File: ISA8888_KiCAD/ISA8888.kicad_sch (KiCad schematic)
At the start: 3 parts, among them J1 Bus_PCI_32bit_Universal, J2 Bus_ISA_16bit

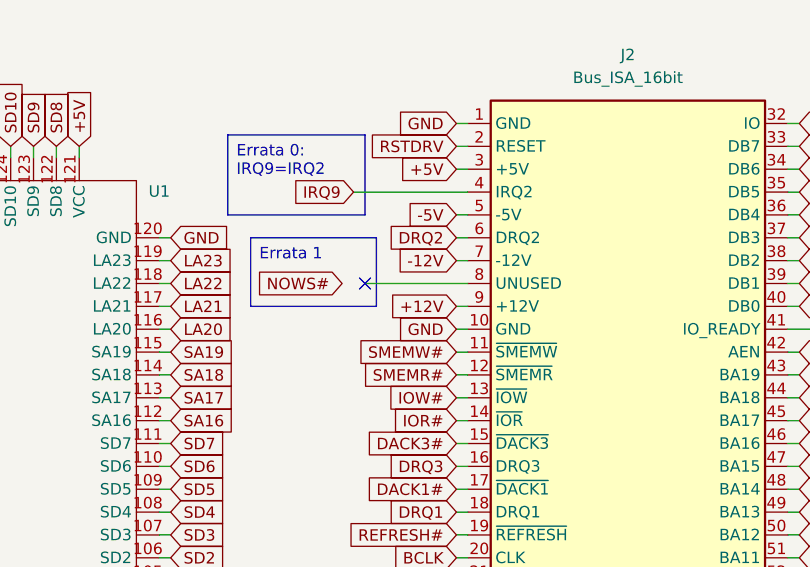
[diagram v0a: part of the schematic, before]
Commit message: Errata 1 and DRQ Pull Down Fix
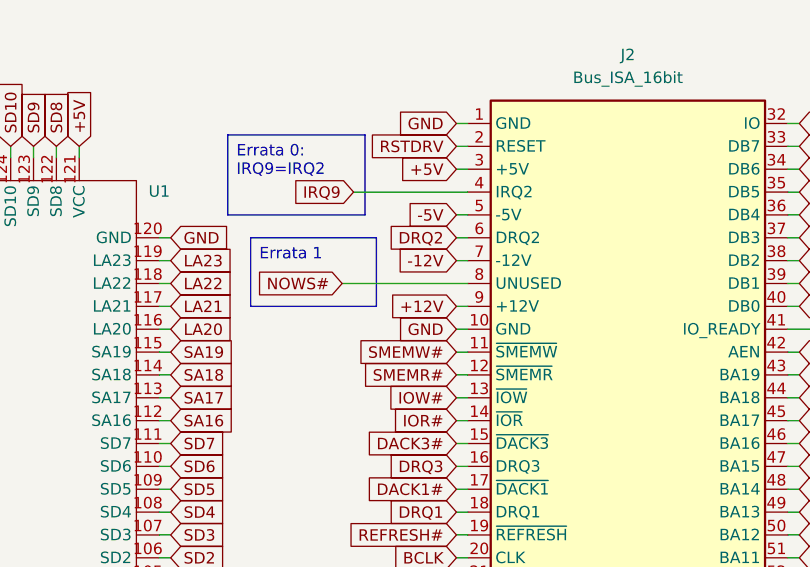
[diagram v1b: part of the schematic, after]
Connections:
- net NOWS#: now also J2.8 (UNUSED)
- no-connect marks 26 -> 25
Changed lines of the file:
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@@
-	)
-	(no_connect
-		(at 281.94 121.92)
 	)
 	(no_connect
@@
 	(wire
 		(pts
-			(xy 281.94 121.92) (xy 293.37 121.92)
-		)
-		(stroke
-			(width 0)
-			(type default)
-		)
-	)
-	(wire
-		(pts
 			(xy 292.1 147.32) (xy 293.37 147.32)
 		)
@@
 		)
 		(stroke
+			(width 0)
+			(type default)
+		)
+	)
+	(wire
+		(pts
+			(xy 279.4 121.92) (xy 293.37 121.92)
+		)
+		(stroke
